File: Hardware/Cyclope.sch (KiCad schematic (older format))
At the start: 0 parts

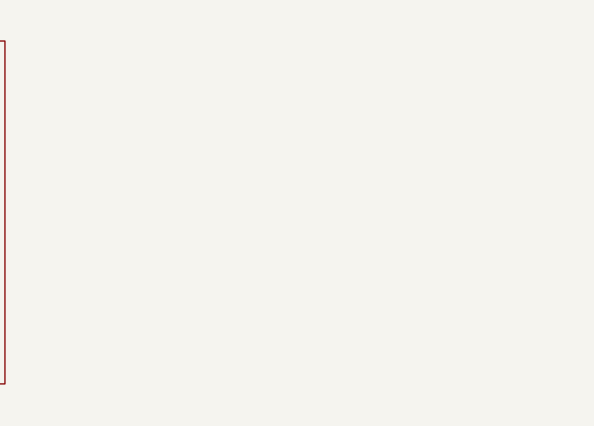
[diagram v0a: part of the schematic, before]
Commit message: [Hardware] Started ADC schematic sheet. Added ADC, voltage regulator and battery voltage sensing.
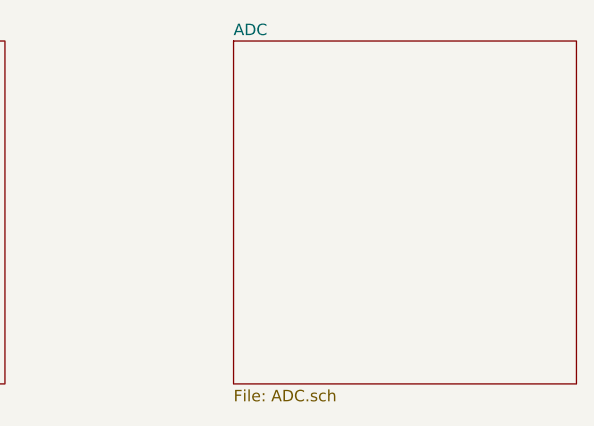
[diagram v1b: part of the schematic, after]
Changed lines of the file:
@@
 $Descr A4 11693 8268
 encoding utf-8
-Sheet 1 3
+Sheet 1 4
 Title "Main page"
 Date "2020-07-27"
@@
 F1 "Raspberry_Pi.sch" 50
 $EndSheet
+$Sheet
+S 7500 2000 1500 1500
+U 5F1FECAE
+F0 "ADC" 50
+F1 "ADC.sch" 50
+$EndSheet
 $EndSCHEMATC

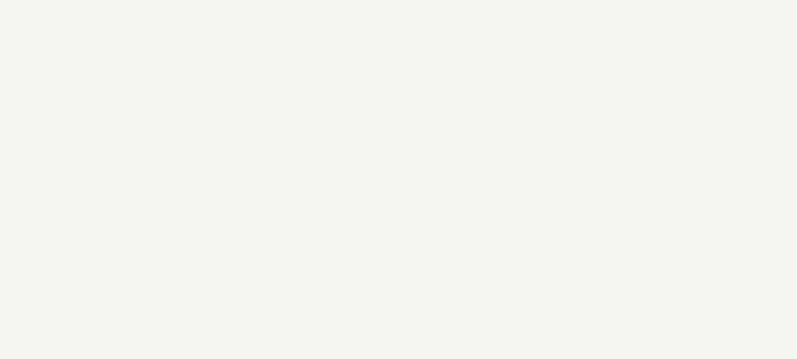
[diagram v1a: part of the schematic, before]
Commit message: [Hardware] Moved servomotors supply parts to main page. Also added servomotors wheels and supports supplies.
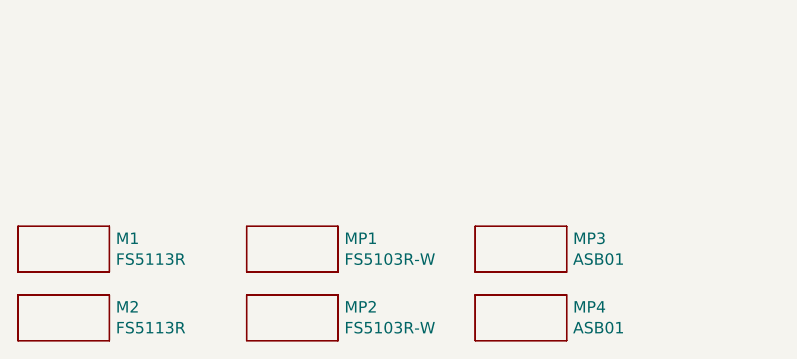
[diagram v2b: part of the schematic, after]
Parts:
- added M1, M2: FS5113R, Supply_Part:Supply_Part, symbol Supply_Part:Supply_Part
- added MP1, MP2: FS5103R-W, Supply_Part:Supply_Part, symbol Supply_Part:Supply_Part
- added MP3, MP4: ASB01, Supply_Part:Supply_Part, symbol Supply_Part:Supply_Part
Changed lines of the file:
@@
 F1 "ADC.sch" 50
 $EndSheet
+$Comp
+L Supply_Part:Supply_Part M?
+U 1 1 5F27E4DF
+P 1200 6400
+AR Path="/5F22814A/5F27E4DF" Ref="M?"  Part="1"
+AR Path="/5F27E4DF" Ref="M2"  Part="1"
+F 0 "M2" H 1428 6446 50  0000 L CNN
+F 1 "FS5113R" H 1428 6355 50  0000 L CNN
+F 2 "Supply_Part:Supply_Part" H 1200 6400 50  0001 C CNN
+F 3 "" H 1200 6400 50  0001 C CNN
+F 4 "Manufacturer" H 1200 6400 50  0001 C CNN "Value2"
+	1    1200 6400
+	1    0    0    -1
+$EndComp
+$Comp
+L Supply_Part:Supply_Part M?
+U 1 1 5F28128C
+P 1200 6100
+AR Path="/5F22814A/5F28128C" Ref="M?"  Part="1"
+AR Path="/5F28128C" Ref="M1"  Part="1"
+F 0 "M1" H 1428 6146 50  0000 L CNN
+F 1 "FS5113R" H 1428 6055 50  0000 L CNN
+F 2 "Supply_Part:Supply_Part" H 1200 6100 50  0001 C CNN
+F 3 "" H 1200 6100 50  0001 C CNN
+F 4 "Feetech" H 1200 6100 50  0001 C CNN "Manufacturer"
+	1    1200 6100
+	1    0    0    -1
+$EndComp
+$Comp
+L Supply_Part:Supply_Part M?
+U 1 1 5F281D4B
+P 2200 6100
+AR Path="/5F22814A/5F281D4B" Ref="M?"  Part="1"
+AR Path="/5F281D4B" Ref="MP1"  Part="1"
+F 0 "MP1" H 2428 6146 50  0000 L CNN
+F 1 "FS5103R-W" H 2428 6055 50  0000 L CNN
+F 2 "Supply_Part:Supply_Part" H 2200 6100 50  0001 C CNN
+F 3 "" H 2200 6100 50  0001 C CNN
+F 4 "Feetech" H 2200 6100 50  0001 C CNN "Manufacturer"
+F 5 "Wheel" H 2200 6100 50  0001 C CNN "Value2"
+	1    2200 6100
+	1    0    0    -1
+$EndComp
+$Comp
+L Supply_Part:Supply_Part M?
+U 1 1 5F2828BE
+P 2200 6400
+AR Path="/5F22814A/5F2828BE" Ref="M?"  Part="1"
+AR Path="/5F2828BE" Ref="MP2"  Part="1"
+F 0 "MP2" H 2428 6446 50  0000 L CNN
+F 1 "FS5103R-W" H 2428 6355 50  0000 L CNN
+F 2 "Supply_Part:Supply_Part" H 2200 6400 50  0001 C CNN
+F 3 "" H 2200 6400 50  0001 C CNN
+F 4 "Feetech" H 2200 6400 50  0001 C CNN "Manufacturer"
+F 5 "Wheel" H 2200 6400 50  0001 C CNN "Value2"
+	1    2200 6400
+	1    0    0    -1
+$EndComp
+$Comp
+L Supply_Part:Supply_Part MP?
+U 1 1 5F283565
+P 3200 6100
+AR Path="/5F22814A/5F283565" Ref="MP?"  Part="1"
+AR Path="/5F283565" Ref="MP3"  Part="1"
+F 0 "MP3" H 3428 6146 50  0000 L CNN
+F 1 "ASB01" H 3428 6055 50  0000 L CNN
+F 2 "Supply_Part:Supply_Part" H 3200 6100 50  0001 C CNN
+F 3 "" H 3200 6100 50  0001 C CNN
+F 4 "Servomotor support" H 3200 6100 50  0001 C CNN "Value2"
+F 5 "https://www.gotronic.fr/art-support-de-servos-asb01-11637.htm" H 3200 6100 50  0001 C CNN "PurchaseLink"
+	1    3200 6100
+	1    0    0    -1
+$EndComp
+$Comp
+L Supply_Part:Supply_Part MP?
+U 1 1 5F283D48
+P 3200 6400
+AR Path="/5F22814A/5F283D48" Ref="MP?"  Part="1"
+AR Path="/5F283D48" Ref="MP4"  Part="1"
+F 0 "MP4" H 3428 6446 50  0000 L CNN
+F 1 "ASB01" H 3428 6355 50  0000 L CNN
+F 2 "Supply_Part:Supply_Part" H 3200 6400 50  0001 C CNN
+F 3 "" H 3200 6400 50  0001 C CNN
+F 4 "Servomotor support" H 3200 6400 50  0001 C CNN "Value2"
+F 5 "https://www.gotronic.fr/art-support-de-servos-asb01-11637.htm" H 3200 6400 50  0001 C CNN "PurchaseLink"
+	1    3200 6400
+	1    0    0    -1
+$EndComp
 $EndSCHEMATC

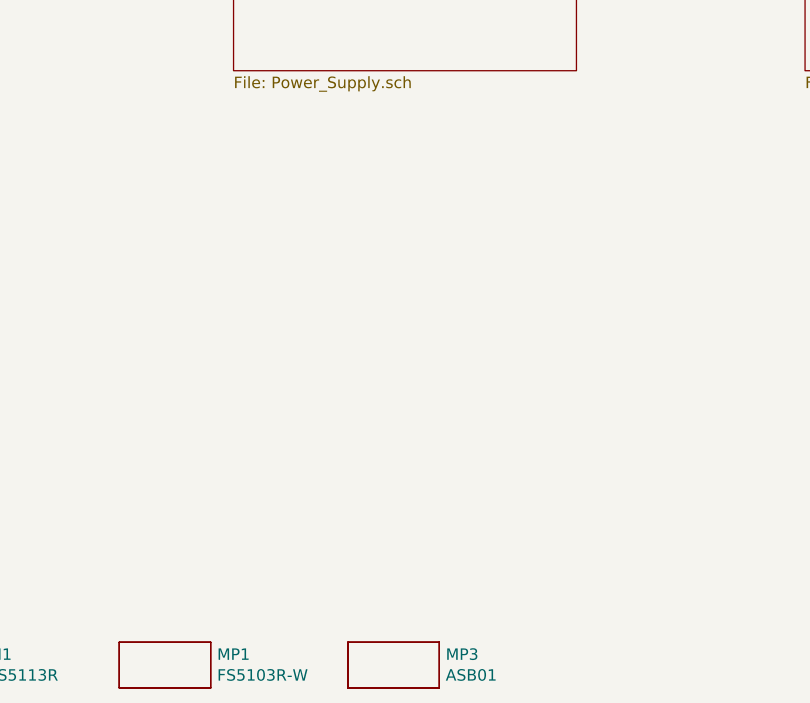
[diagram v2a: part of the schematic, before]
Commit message: [Hardware] Added camera board.
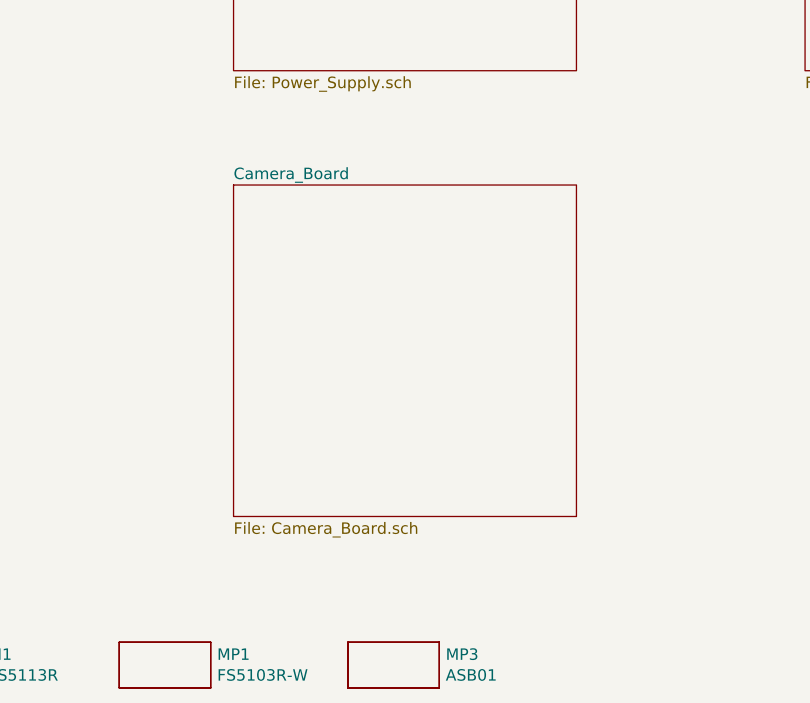
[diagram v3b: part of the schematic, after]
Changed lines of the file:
@@
 $Descr A4 11693 8268
 encoding utf-8
-Sheet 1 4
+Sheet 1 5
 Title "Main page"
 Date "2020-07-27"
@@
 	1    0    0    -1
 $EndComp
+$Sheet
+S 2500 4000 1500 1450
+U 5F288D93
+F0 "Camera_Board" 50
+F1 "Camera_Board.sch" 50
+$EndSheet
 $EndSCHEMATC

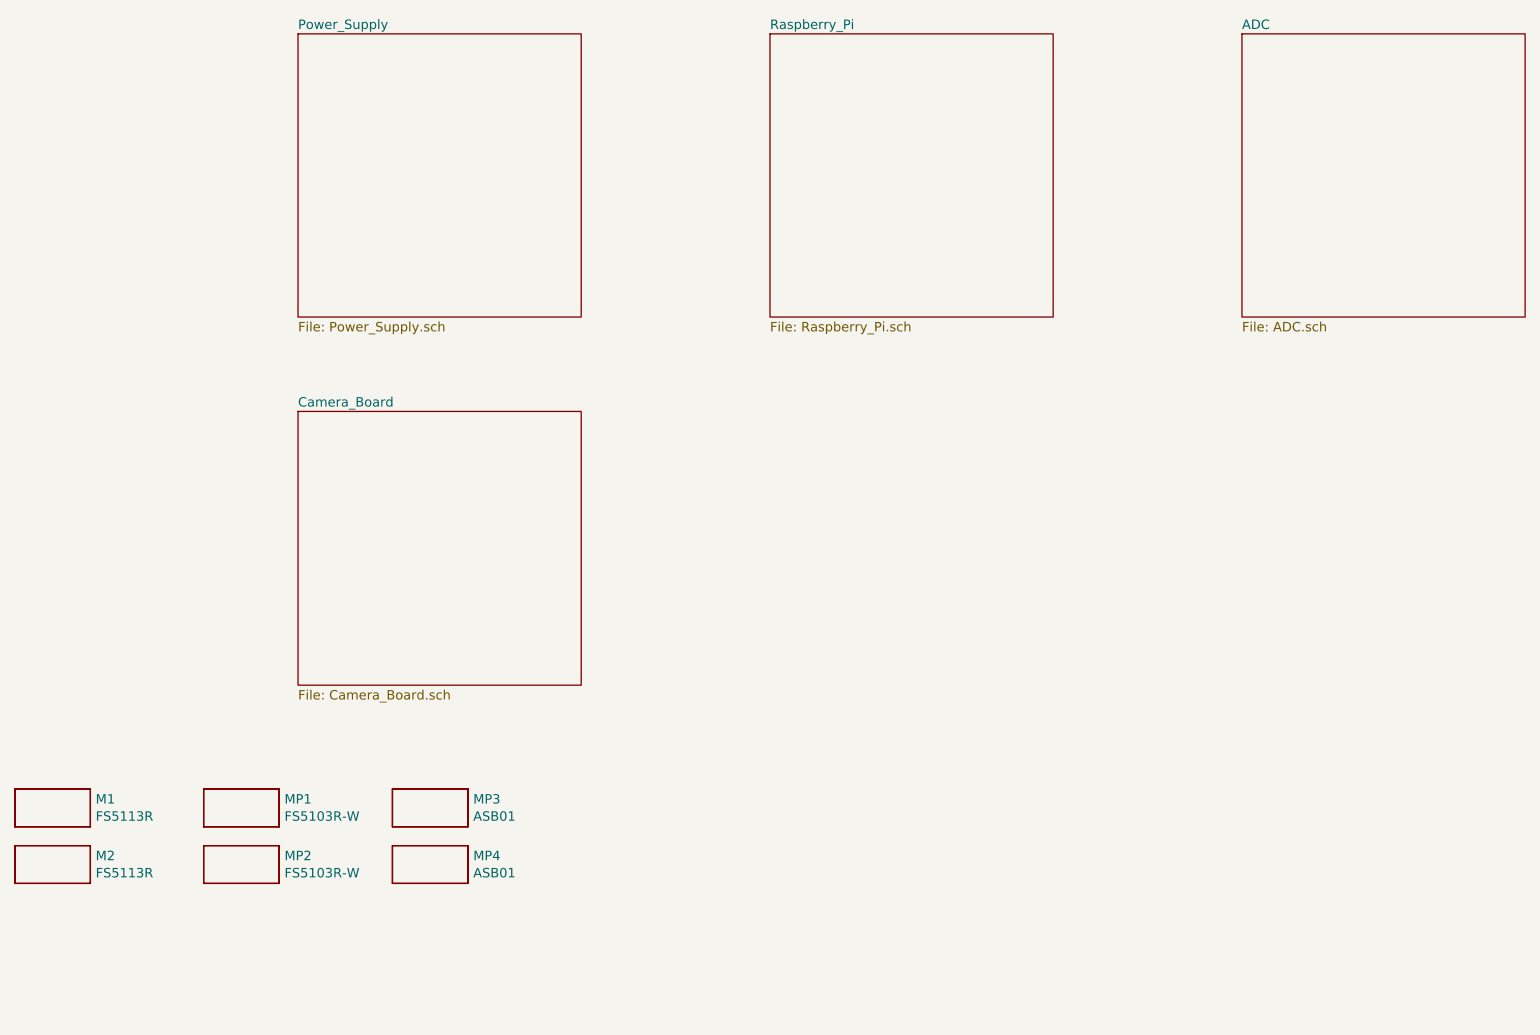
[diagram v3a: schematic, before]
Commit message: [Hardware] Added Raspberry Pi mounting holes to schematic.
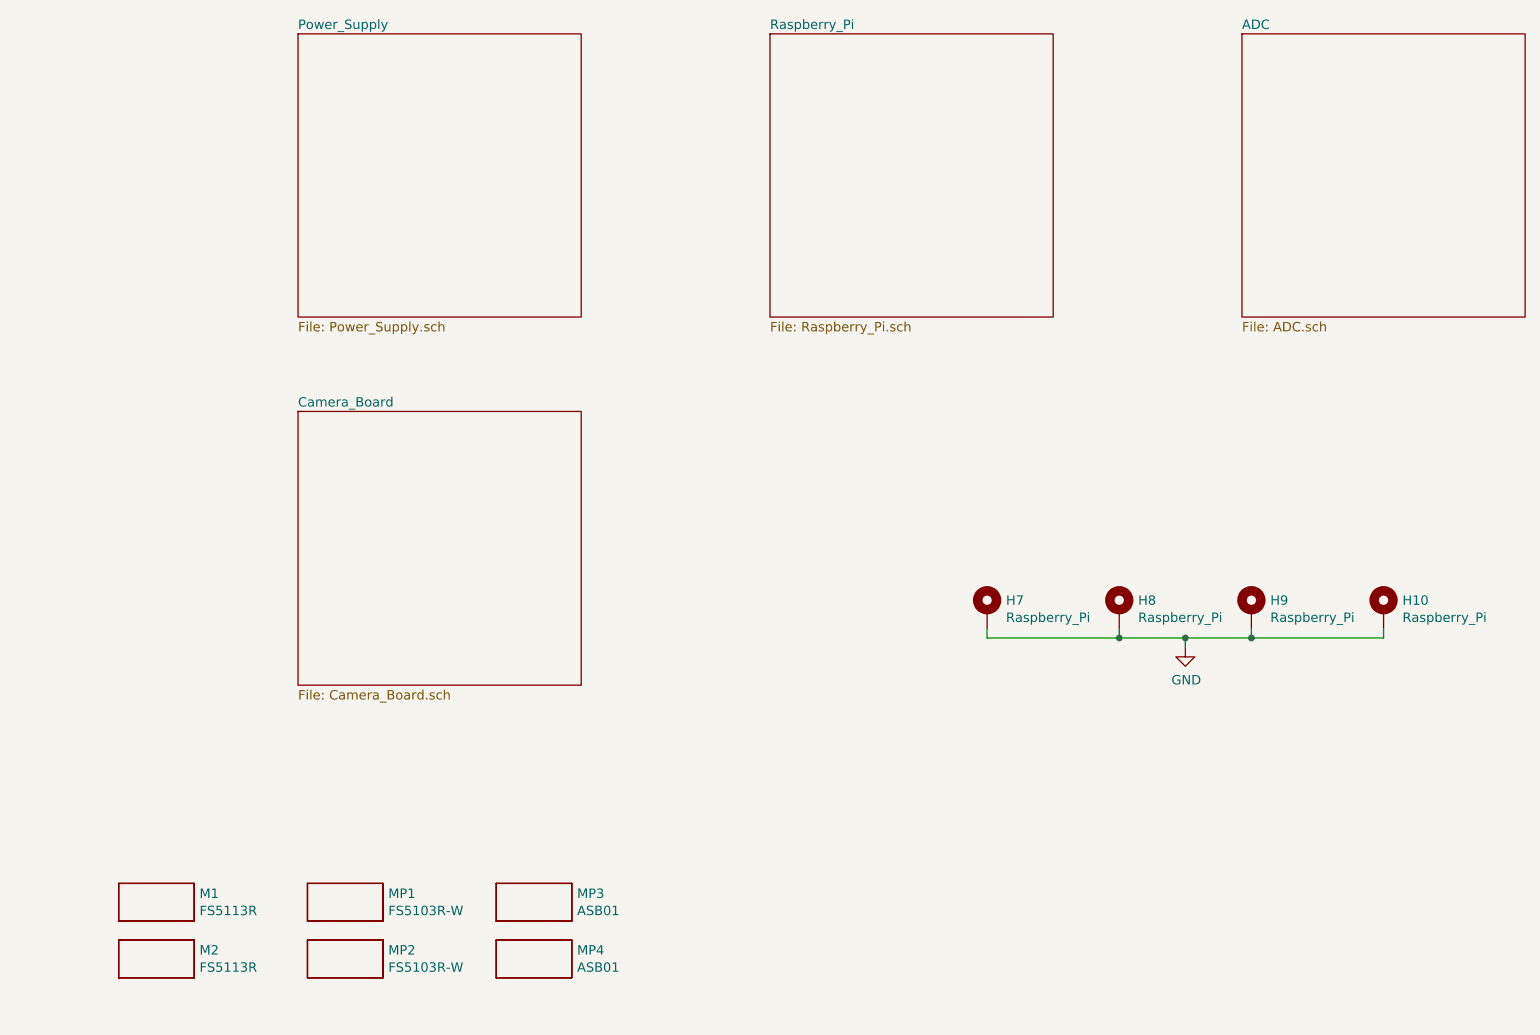
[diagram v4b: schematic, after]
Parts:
- added H10, H7, H8, H9: Raspberry_Pi, MountingHole:MountingHole_3.2mm_M3_Pad, symbol Mechanical:MountingHole_Pad
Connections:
- new net GND: H10.1, H7.1, H8.1, H9.1
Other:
- moved on the sheet: M1, M2, MP1, MP2, MP3, MP4
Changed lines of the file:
@@
 L Supply_Part:Supply_Part M?
 U 1 1 5F27E4DF
-P 1200 6400
+P 1750 6900
 AR Path="/5F22814A/5F27E4DF" Ref="M?"  Part="1"
 AR Path="/5F27E4DF" Ref="M2"  Part="1"
-F 0 "M2" H 1428 6446 50  0000 L CNN
-F 1 "FS5113R" H 1428 6355 50  0000 L CNN
-F 2 "Supply_Part:Supply_Part" H 1200 6400 50  0001 C CNN
-F 3 "" H 1200 6400 50  0001 C CNN
-F 4 "Manufacturer" H 1200 6400 50  0001 C CNN "Value2"
-	1    1200 6400
+F 0 "M2" H 1978 6946 50  0000 L CNN
+F 1 "FS5113R" H 1978 6855 50  0000 L CNN
+F 2 "Supply_Part:Supply_Part" H 1750 6900 50  0001 C CNN
+F 3 "" H 1750 6900 50  0001 C CNN
+F 4 "Manufacturer" H 1750 6900 50  0001 C CNN "Value2"
+	1    1750 6900
 	1    0    0    -1
 $EndComp
@@
 L Supply_Part:Supply_Part M?
 U 1 1 5F28128C
-P 1200 6100
+P 1750 6600
 AR Path="/5F22814A/5F28128C" Ref="M?"  Part="1"
 AR Path="/5F28128C" Ref="M1"  Part="1"
-F 0 "M1" H 1428 6146 50  0000 L CNN
-F 1 "FS5113R" H 1428 6055 50  0000 L CNN
-F 2 "Supply_Part:Supply_Part" H 1200 6100 50  0001 C CNN
-F 3 "" H 1200 6100 50  0001 C CNN
-F 4 "Feetech" H 1200 6100 50  0001 C CNN "Manufacturer"
-	1    1200 6100
+F 0 "M1" H 1978 6646 50  0000 L CNN
+F 1 "FS5113R" H 1978 6555 50  0000 L CNN
+F 2 "Supply_Part:Supply_Part" H 1750 6600 50  0001 C CNN
+F 3 "" H 1750 6600 50  0001 C CNN
+F 4 "Feetech" H 1750 6600 50  0001 C CNN "Manufacturer"
+	1    1750 6600
 	1    0    0    -1
 $EndComp
@@
 L Supply_Part:Supply_Part M?
 U 1 1 5F281D4B
-P 2200 6100
+P 2750 6600
 AR Path="/5F22814A/5F281D4B" Ref="M?"  Part="1"
 AR Path="/5F281D4B" Ref="MP1"  Part="1"
-F 0 "MP1" H 2428 6146 50  0000 L CNN
-F 1 "FS5103R-W" H 2428 6055 50  0000 L CNN
-F 2 "Supply_Part:Supply_Part" H 2200 6100 50  0001 C CNN
-F 3 "" H 2200 6100 50  0001 C CNN
-F 4 "Feetech" H 2200 6100 50  0001 C CNN "Manufacturer"
-F 5 "Wheel" H 2200 6100 50  0001 C CNN "Value2"
-	1    2200 6100
+F 0 "MP1" H 2978 6646 50  0000 L CNN
+F 1 "FS5103R-W" H 2978 6555 50  0000 L CNN
+F 2 "Supply_Part:Supply_Part" H 2750 6600 50  0001 C CNN
+F 3 "" H 2750 6600 50  0001 C CNN
+F 4 "Feetech" H 2750 6600 50  0001 C CNN "Manufacturer"
+F 5 "Wheel" H 2750 6600 50  0001 C CNN "Value2"
+	1    2750 6600
 	1    0    0    -1
 $EndComp
@@
 L Supply_Part:Supply_Part M?
 U 1 1 5F2828BE
-P 2200 6400
+P 2750 6900
 AR Path="/5F22814A/5F2828BE" Ref="M?"  Part="1"
 AR Path="/5F2828BE" Ref="MP2"  Part="1"
-F 0 "MP2" H 2428 6446 50  0000 L CNN
-F 1 "FS5103R-W" H 2428 6355 50  0000 L CNN
-F 2 "Supply_Part:Supply_Part" H 2200 6400 50  0001 C CNN
-F 3 "" H 2200 6400 50  0001 C CNN
-F 4 "Feetech" H 2200 6400 50  0001 C CNN "Manufacturer"
-F 5 "Wheel" H 2200 6400 50  0001 C CNN "Value2"
-	1    2200 6400
+F 0 "MP2" H 2978 6946 50  0000 L CNN
+F 1 "FS5103R-W" H 2978 6855 50  0000 L CNN
+F 2 "Supply_Part:Supply_Part" H 2750 6900 50  0001 C CNN
+F 3 "" H 2750 6900 50  0001 C CNN
+F 4 "Feetech" H 2750 6900 50  0001 C CNN "Manufacturer"
+F 5 "Wheel" H 2750 6900 50  0001 C CNN "Value2"
+	1    2750 6900
 	1    0    0    -1
 $EndComp
@@
 L Supply_Part:Supply_Part MP?
 U 1 1 5F283565
-P 3200 6100
+P 3750 6600
 AR Path="/5F22814A/5F283565" Ref="MP?"  Part="1"
 AR Path="/5F283565" Ref="MP3"  Part="1"
-F 0 "MP3" H 3428 6146 50  0000 L CNN
-F 1 "ASB01" H 3428 6055 50  0000 L CNN
-F 2 "Supply_Part:Supply_Part" H 3200 6100 50  0001 C CNN
-F 3 "" H 3200 6100 50  0001 C CNN
-F 4 "Servomotor support" H 3200 6100 50  0001 C CNN "Value2"
-F 5 "https://www.gotronic.fr/art-support-de-servos-asb01-11637.htm" H 3200 6100 50  0001 C CNN "PurchaseLink"
-	1    3200 6100
+F 0 "MP3" H 3978 6646 50  0000 L CNN
+F 1 "ASB01" H 3978 6555 50  0000 L CNN
+F 2 "Supply_Part:Supply_Part" H 3750 6600 50  0001 C CNN
+F 3 "" H 3750 6600 50  0001 C CNN
+F 4 "Servomotor support" H 3750 6600 50  0001 C CNN "Value2"
+F 5 "https://www.gotronic.fr/art-support-de-servos-asb01-11637.htm" H 3750 6600 50  0001 C CNN "PurchaseLink"
+	1    3750 6600
 	1    0    0    -1
 $EndComp
@@
 L Supply_Part:Supply_Part MP?
 U 1 1 5F283D48
-P 3200 6400
+P 3750 6900
 AR Path="/5F22814A/5F283D48" Ref="MP?"  Part="1"
 AR Path="/5F283D48" Ref="MP4"  Part="1"
-F 0 "MP4" H 3428 6446 50  0000 L CNN
-F 1 "ASB01" H 3428 6355 50  0000 L CNN
-F 2 "Supply_Part:Supply_Part" H 3200 6400 50  0001 C CNN
-F 3 "" H 3200 6400 50  0001 C CNN
-F 4 "Servomotor support" H 3200 6400 50  0001 C CNN "Value2"
-F 5 "https://www.gotronic.fr/art-support-de-servos-asb01-11637.htm" H 3200 6400 50  0001 C CNN "PurchaseLink"
-	1    3200 6400
+F 0 "MP4" H 3978 6946 50  0000 L CNN
+F 1 "ASB01" H 3978 6855 50  0000 L CNN
+F 2 "Supply_Part:Supply_Part" H 3750 6900 50  0001 C CNN
+F 3 "" H 3750 6900 50  0001 C CNN
+F 4 "Servomotor support" H 3750 6900 50  0001 C CNN "Value2"
+F 5 "https://www.gotronic.fr/art-support-de-servos-asb01-11637.htm" H 3750 6900 50  0001 C CNN "PurchaseLink"
+	1    3750 6900
 	1    0    0    -1
 $EndComp
@@
 F1 "Camera_Board.sch" 50
 $EndSheet
+$Comp
+L Mechanical:MountingHole_Pad H7
+U 1 1 5F3532F6
+P 6150 5050
+F 0 "H7" H 6250 5099 50  0000 L CNN
+F 1 "Raspberry_Pi" H 6250 5008 50  0000 L CNN
+F 2 "MountingHole:MountingHole_3.2mm_M3_Pad" H 6150 5050 50  0001 C CNN
+F 3 "~" H 6150 5050 50  0001 C CNN
+	1    6150 5050
+	1    0    0    -1
+$EndComp
+$Comp
+L Mechanical:MountingHole_Pad H8
+U 1 1 5F353CDE
+P 6850 5050
+F 0 "H8" H 6950 5099 50  0000 L CNN
+F 1 "Raspberry_Pi" H 6950 5008 50  0000 L CNN
+F 2 "MountingHole:MountingHole_3.2mm_M3_Pad" H 6850 5050 50  0001 C CNN
+F 3 "~" H 6850 5050 50  0001 C CNN
+	1    6850 5050
+	1    0    0    -1
+$EndComp
+$Comp
+L Mechanical:MountingHole_Pad H9
+U 1 1 5F35418A
+P 7550 5050
+F 0 "H9" H 7650 5099 50  0000 L CNN
+F 1 "Raspberry_Pi" H 7650 5008 50  0000 L CNN
+F 2 "MountingHole:MountingHole_3.2mm_M3_Pad" H 7550 5050 50  0001 C CNN
+F 3 "~" H 7550 5050 50  0001 C CNN
+	1    7550 5050
+	1    0    0    -1
+$EndComp
+$Comp
+L Mechanical:MountingHole_Pad H10
+U 1 1 5F3543C8
+P 8250 5050
+F 0 "H10" H 8350 5099 50  0000 L CNN
+F 1 "Raspberry_Pi" H 8350 5008 50  0000 L CNN
+F 2 "MountingHole:MountingHole_3.2mm_M3_Pad" H 8250 5050 50  0001 C CNN
+F 3 "~" H 8250 5050 50  0001 C CNN
+	1    8250 5050
+	1    0    0    -1
+$EndComp
+$Comp
+L power:GND #PWR018
+U 1 1 5F3568FB
+P 7200 5250
+F 0 "#PWR018" H 7200 5000 50  0001 C CNN
+F 1 "GND" H 7205 5077 50  0000 C CNN
+F 2 "" H 7200 5250 50  0001 C CNN
+F 3 "" H 7200 5250 50  0001 C CNN
+	1    7200 5250
+	1    0    0    -1
+$EndComp
+Wire Wire Line
+	6150 5150 6150 5200
+Wire Wire Line
+	6150 5200 6850 5200
+Wire Wire Line
+	6850 5200 6850 5150
+Wire Wire Line
+	6850 5200 7200 5200
+Wire Wire Line
+	7200 5200 7200 5250
+Connection ~ 6850 5200
+Wire Wire Line
+	7200 5200 7550 5200
+Connection ~ 7200 5200
+Wire Wire Line
+	7550 5200 7550 5150
+Connection ~ 7550 5200
+Wire Wire Line
+	8250 5200 8250 5150
+Wire Wire Line
+	7550 5200 8250 5200
 $EndSCHEMATC
